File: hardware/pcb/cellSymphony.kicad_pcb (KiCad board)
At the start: 2 copper layers, 107.2 x 127 mm, 11 parts, among them J1 NeoTrellis_Conn, SW1 RotaryEncoder_Switch, SW2 RotaryEncoder_Switch, SW3 RotaryEncoder_Switch, SW4 RotaryEncoder_Switch, U1 Raspberry Zero 2 W, U2 SSD1351, U3 USB-C, U4 PCM5102a, U5 NeoKey

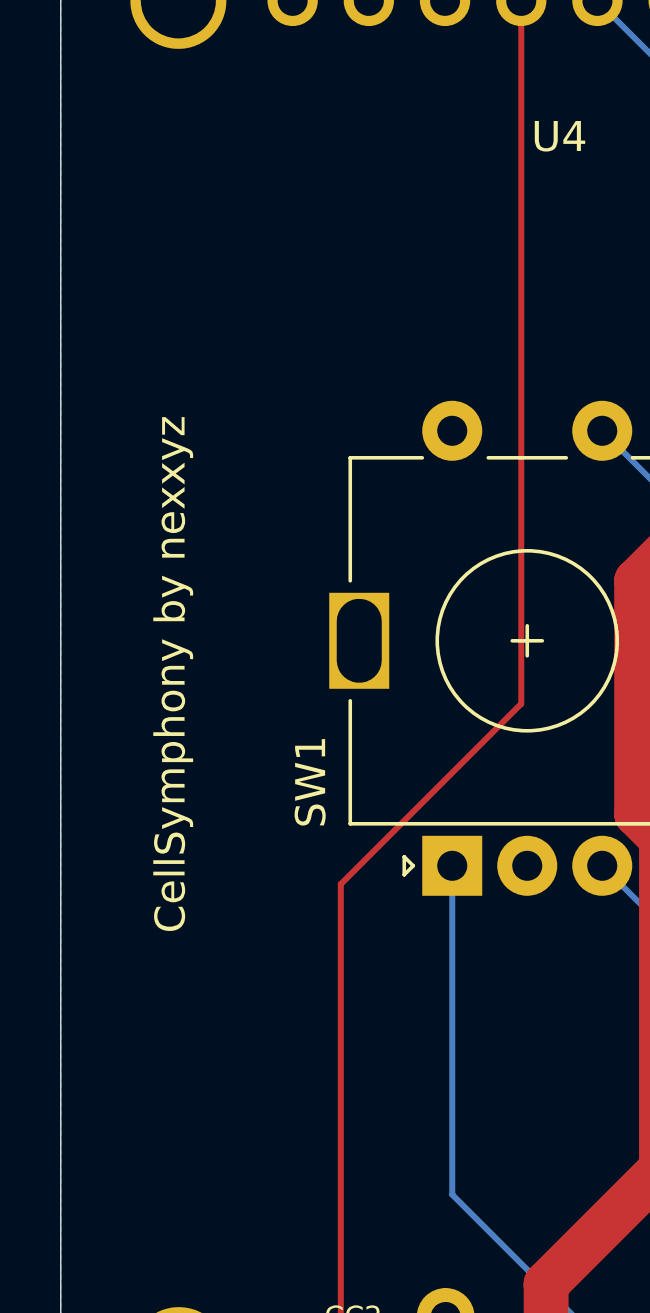
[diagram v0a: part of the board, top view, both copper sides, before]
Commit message: Add hardware branding and assembly references
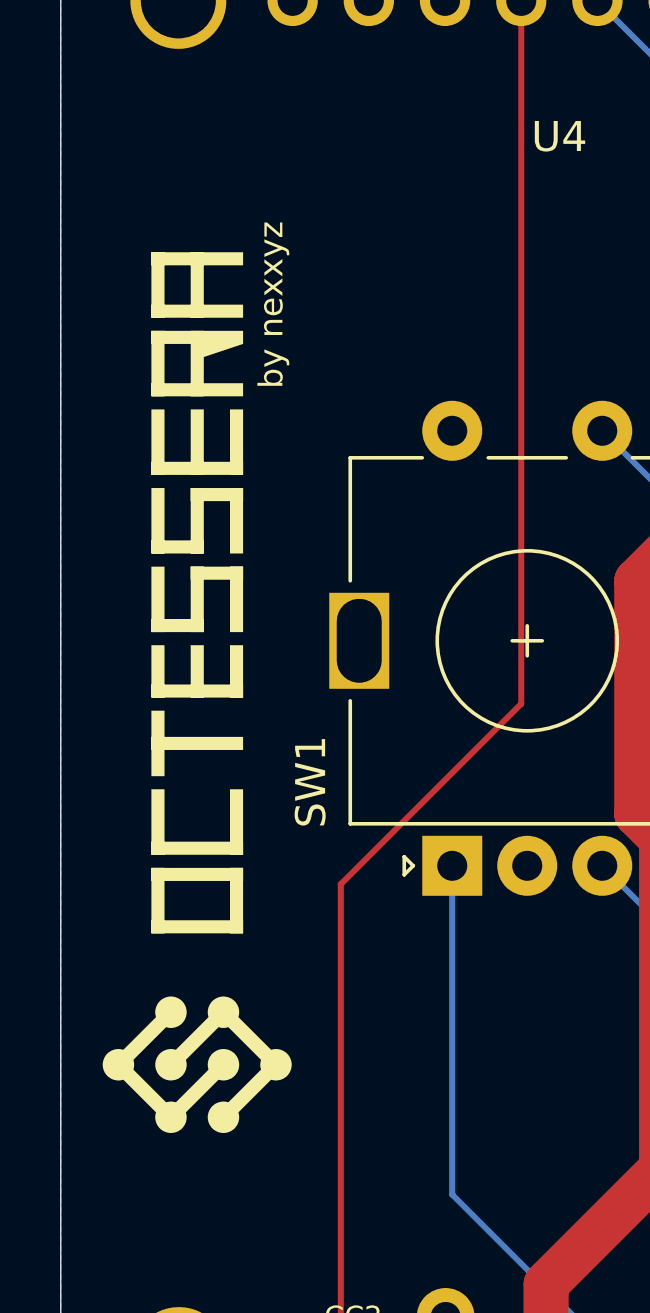
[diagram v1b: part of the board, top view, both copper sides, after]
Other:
- board text added: "by nexxyz"
- board text removed: "CellSymphony by nexxyz"
